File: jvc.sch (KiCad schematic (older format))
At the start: 14 parts, among them J1 AV PCB, J2 Main PCB, J3 VGA, SW1 SW_SPST

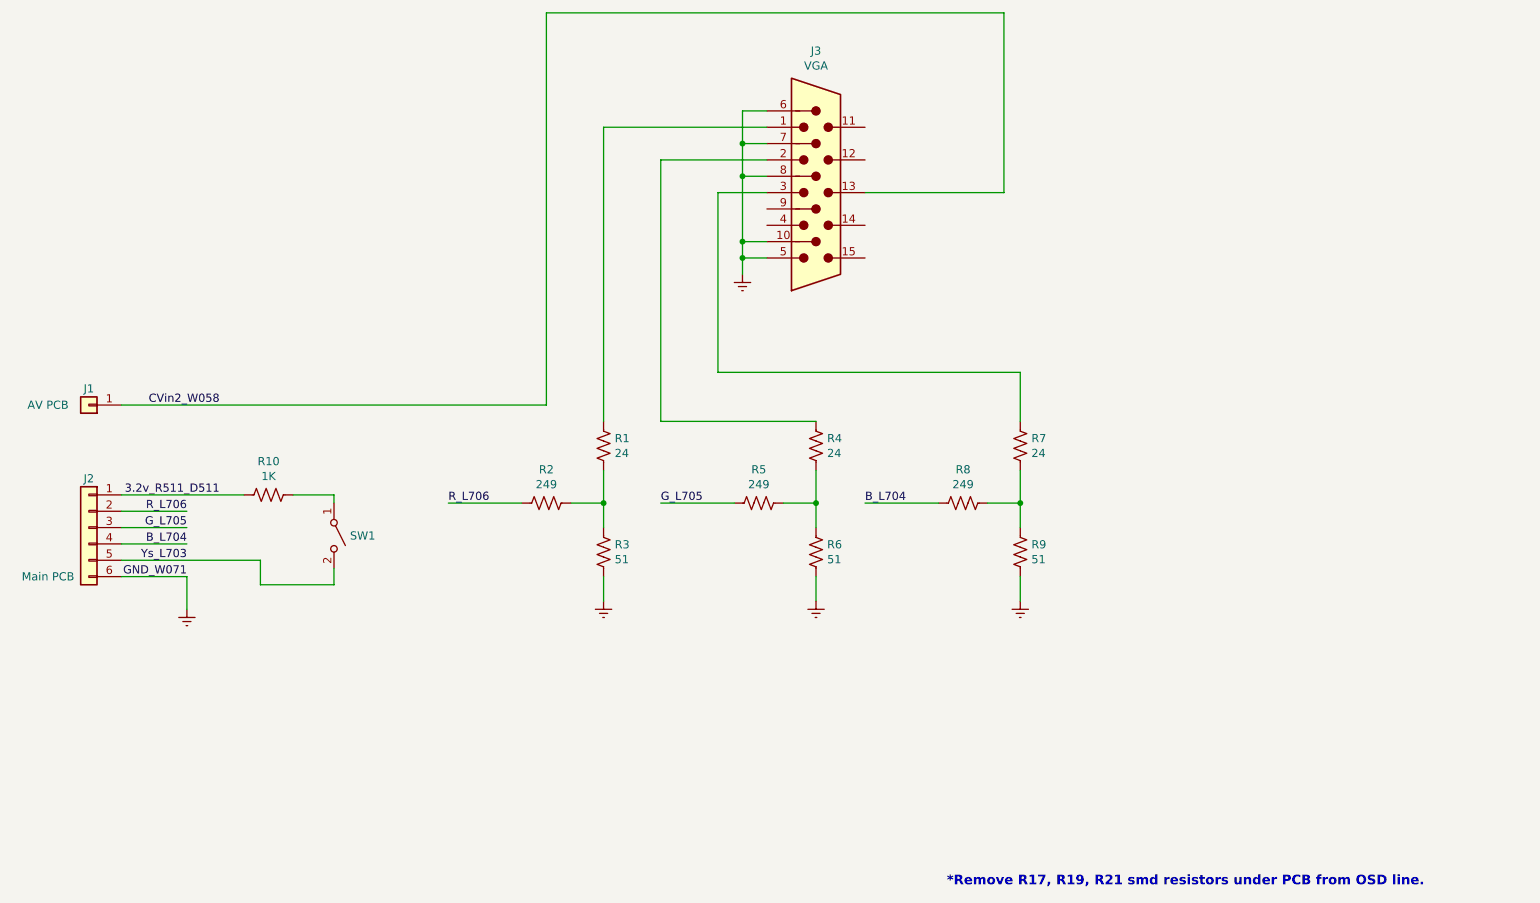
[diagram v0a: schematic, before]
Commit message: Turnout Not 0.5Vpp
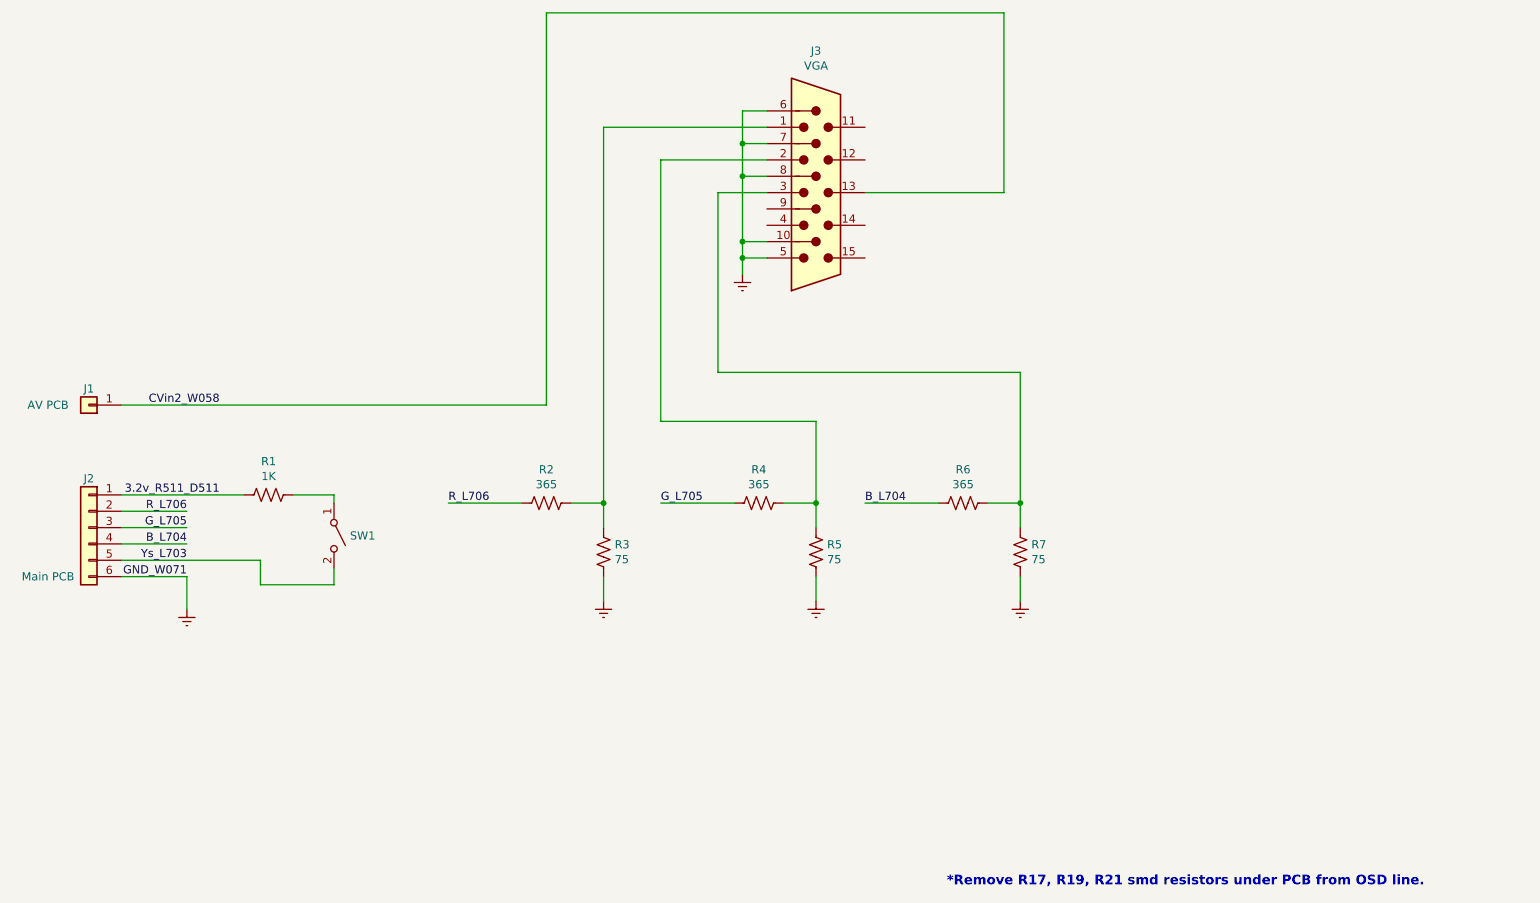
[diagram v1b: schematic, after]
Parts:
- removed R1, R4, R7: 24, symbol Device:R_US
- R2: value 249 -> 365
- R3: value 51 -> 75
- R4: renamed from R5; value 249 -> 365
- R5: renamed from R6; value 51 -> 75
- R6: renamed from R8; value 249 -> 365
- R7: renamed from R9; value 51 -> 75
- renumbered R10 to R1
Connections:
- net at J3.1: now also R2.1, R3.1
- net at J3.3: now also R6.1, R7.1
- net at J3.2: now also R4.1, R5.1
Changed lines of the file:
@@
 $EndDescr
-$Comp
-L Device:R_US R1
-U 1 1 5E6B4719
-P 4950 4000
-F 0 "R1" H 5018 4046 50  0000 L CNN
-F 1 "24" H 5018 3955 50  0000 L CNN
-F 2 "" V 4990 3990 50  0001 C CNN
-F 3 "~" H 4950 4000 50  0001 C CNN
-	1    4950 4000
-	1    0    0    -1
-$EndComp
 $Comp
 L Device:R_US R2
@@
 P 4600 4350
 F 0 "R2" V 4395 4350 50  0000 C CNN
-F 1 "249" V 4486 4350 50  0000 C CNN
+F 1 "365" V 4486 4350 50  0000 C CNN
 F 2 "" V 4640 4340 50  0001 C CNN
 F 3 "~" H 4600 4350 50  0001 C CNN
@@
 P 4950 4650
 F 0 "R3" H 5018 4696 50  0000 L CNN
-F 1 "51" H 5018 4605 50  0000 L CNN
+F 1 "75" H 5018 4605 50  0000 L CNN
 F 2 "" V 4990 4640 50  0001 C CNN
 F 3 "~" H 4950 4650 50  0001 C CNN
@@
 	1    0    0    -1
 $EndComp
-Wire Wire Line
-	4950 4150 4950 4350
 Connection ~ 4950 4350
 Wire Wire Line
@@
 $EndComp
 $Comp
-L Device:R_US R7
-U 1 1 5E6CEC38
-P 7500 4000
-F 0 "R7" H 7568 4046 50  0000 L CNN
-F 1 "24" H 7568 3955 50  0000 L CNN
-F 2 "" V 7540 3990 50  0001 C CNN
-F 3 "~" H 7500 4000 50  0001 C CNN
-	1    7500 4000
-	1    0    0    -1
-$EndComp
-$Comp
-L Device:R_US R8
+L Device:R_US R6
 U 1 1 5E6CEC42
 P 7150 4350
-F 0 "R8" V 6945 4350 50  0000 C CNN
-F 1 "249" V 7036 4350 50  0000 C CNN
+F 0 "R6" V 6945 4350 50  0000 C CNN
+F 1 "365" V 7036 4350 50  0000 C CNN
 F 2 "" V 7190 4340 50  0001 C CNN
 F 3 "~" H 7150 4350 50  0001 C CNN
@@
 $EndComp
 $Comp
-L Device:R_US R9
+L Device:R_US R7
 U 1 1 5E6CEC4C
 P 7500 4650
-F 0 "R9" H 7568 4696 50  0000 L CNN
-F 1 "51" H 7568 4605 50  0000 L CNN
+F 0 "R7" H 7568 4696 50  0000 L CNN
+F 1 "75" H 7568 4605 50  0000 L CNN
 F 2 "" V 7540 4640 50  0001 C CNN
 F 3 "~" H 7500 4650 50  0001 C CNN
@@
 	1    0    0    -1
 $EndComp
-Wire Wire Line
-	7500 4150 7500 4350
 Connection ~ 7500 4350
 Wire Wire Line
@@
 	7300 4350 7500 4350
 $Comp
-L Device:R_US R4
-U 1 1 5E6D13FF
-P 6250 4000
-F 0 "R4" H 6318 4046 50  0000 L CNN
-F 1 "24" H 6318 3955 50  0000 L CNN
-F 2 "" V 6290 3990 50  0001 C CNN
-F 3 "~" H 6250 4000 50  0001 C CNN
-	1    6250 4000
-	1    0    0    -1
-$EndComp
-$Comp
 L Device:R_US R5
-U 1 1 5E6D1409
-P 5900 4350
-F 0 "R5" V 5695 4350 50  0000 C CNN
-F 1 "249" V 5786 4350 50  0000 C CNN
-F 2 "" V 5940 4340 50  0001 C CNN
-F 3 "~" H 5900 4350 50  0001 C CNN
-	1    5900 4350
-	0    1    1    0
-$EndComp
-$Comp
-L Device:R_US R6
 U 1 1 5E6D1413
 P 6250 4650
-F 0 "R6" H 6318 4696 50  0000 L CNN
-F 1 "51" H 6318 4605 50  0000 L CNN
+F 0 "R5" H 6318 4696 50  0000 L CNN
+F 1 "75" H 6318 4605 50  0000 L CNN
 F 2 "" V 6290 4640 50  0001 C CNN
 F 3 "~" H 6250 4650 50  0001 C CNN
@@
 	1    0    0    -1
 $EndComp
-Wire Wire Line
-	6250 4150 6250 4350
 Connection ~ 6250 4350
 Wire Wire Line
@@
 $EndComp
 Wire Wire Line
-	4950 3850 4950 2050
-Wire Wire Line
 	4950 2050 5950 2050
 Wire Wire Line
@@
 Wire Wire Line
 	5300 2250 5950 2250
-Wire Wire Line
-	7500 3850 7500 3550
 Wire Wire Line
 	7500 3550 5650 3550
@@
 $EndComp
 $Comp
-L Device:R_US R10
+L Device:R_US R1
 U 1 1 5E712B9B
 P 2900 4300
-F 0 "R10" V 2695 4300 50  0000 C CNN
+F 0 "R1" V 2695 4300 50  0000 C CNN
 F 1 "1K" V 2786 4300 50  0000 C CNN
 F 2 "" V 2940 4290 50  0001 C CNN
@@
 	5800 1950 5800 2150
 Connection ~ 5800 2150
+Wire Wire Line
+	7500 3550 7500 4350
+Wire Wire Line
+	6250 3850 6250 4350
+Wire Wire Line
+	4950 2050 4950 4350
+$Comp
+L Device:R_US R4
+U 1 1 5E6D1409
+P 5900 4350
+F 0 "R4" V 5695 4350 50  0000 C CNN
+F 1 "365" V 5786 4350 50  0000 C CNN
+F 2 "" V 5940 4340 50  0001 C CNN
+F 3 "~" H 5900 4350 50  0001 C CNN
+	1    5900 4350
+	0    1    1    0
+$EndComp
 $EndSCHEMATC

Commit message: Move RGB on input 1 and DPDT sw enable CVBS input in RGB mode for csync
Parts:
- removed SW1: SW_SPST, symbol Switch:SW_SPST
- added SW1: SW_DPST, symbol Switch:SW_DPST
- J1: symbol Connector_Generic:Conn_01x01 -> Connector_Generic:Conn_01x04
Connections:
- net GNDREF: now also J1.1 (Pin_1)
- net Ys_L703: now also SW1.2
- net at R1.1: now also SW1.1
- net CVin2_W058 renamed CVin1_D815
- net CVin1_D815: now also J1.4 (Pin_4); no longer J1.1 (Pin_1)
- new net S-Video_J801pin5: J1.3 (Pin_3), SW1.4
- new net S-Video_J801pin6: J1.2 (Pin_2), SW1.3
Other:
- note added: "SW1 toggle between\nS-Video & RGB\nBoth share same audio in"
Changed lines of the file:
@@
 B_L704
 $Comp
-L Connector_Generic:Conn_01x01 J1
+L Connector_Generic:Conn_01x04 J1
 U 1 1 5E6BABC1
 P 1800 3750
-F 0 "J1" H 1800 3650 50  0000 C CNN
+F 0 "J1" H 1800 3450 50  0000 C CNN
 F 1 "AV PCB" H 2050 3750 50  0000 C CNN
 F 2 "" H 1800 3750 50  0001 C CNN
@@
 Wire Wire Line
 	2000 4800 2400 4800
-Text Label 2600 3750 2    50   ~ 0
-CVin2_W058
+Text Label 2600 3550 2    50   ~ 0
+CVin1_D815
 Wire Wire Line
 	4750 4350 4950 4350
@@
 	5650 2450 5950 2450
 Wire Wire Line
-	4600 3750 4600 1350
-Wire Wire Line
 	4600 1350 7400 1350
 Wire Wire Line
@@
 	7400 2450 6550 2450
 Wire Wire Line
-	2000 3750 4600 3750
+	2000 3550 4600 3550
 Text Notes 7050 6700 0    59   ~ 12
 *Remove R17, R19, R21 smd resistors under PCB from OSD line.
-$Comp
-L Switch:SW_SPST SW1
-U 1 1 5E711972
-P 3300 4550
-F 0 "SW1" V 3300 4648 50  0000 L CNN
-F 1 "SW_SPST" V 3345 4648 50  0001 L CNN
-F 2 "" H 3300 4550 50  0001 C CNN
-F 3 "~" H 3300 4550 50  0001 C CNN
-	1    3300 4550
-	0    1    1    0
-$EndComp
 $Comp
 L Device:R_US R1
@@
 	2000 4300 2750 4300
 Wire Wire Line
-	3050 4300 3300 4300
-Wire Wire Line
-	3300 4300 3300 4350
-Wire Wire Line
-	2850 4700 2850 4850
-Wire Wire Line
-	2850 4850 3300 4850
-Wire Wire Line
-	3300 4850 3300 4750
-Wire Wire Line
-	2000 4700 2850 4700
-Wire Wire Line
 	5950 2350 5800 2350
 $Comp
@@
 	0    1    1    0
 $EndComp
+$Comp
+L Switch:SW_DPST SW1
+U 1 1 5E8D0B90
+P 3400 4200
+F 0 "SW1" H 3400 4525 50  0000 C CNN
+F 1 "SW_DPST" H 3400 4434 50  0000 C CNN
+F 2 "" H 3400 4200 50  0001 C CNN
+F 3 "~" H 3400 4200 50  0001 C CNN
+	1    3400 4200
+	1    0    0    -1
+$EndComp
+$Comp
+L power:GNDREF #PWR?
+U 1 1 5E8D572D
+P 2400 4000
+F 0 "#PWR?" H 2400 3750 50  0001 C CNN
+F 1 "GNDREF" H 2405 3827 50  0001 C CNN
+F 2 "" H 2400 4000 50  0001 C CNN
+F 3 "" H 2400 4000 50  0001 C CNN
+	1    2400 4000
+	1    0    0    -1
+$EndComp
+Wire Wire Line
+	2400 3850 2400 4000
+Wire Wire Line
+	2000 3850 2400 3850
+Wire Wire Line
+	3050 4300 3200 4300
+Wire Wire Line
+	3600 4700 3600 4300
+Wire Wire Line
+	2000 4700 3600 4700
+Wire Wire Line
+	4600 3550 4600 1350
+Wire Wire Line
+	2000 3650 3600 3650
+Wire Wire Line
+	3600 3650 3600 4100
+Wire Wire Line
+	2000 3750 3200 3750
+Wire Wire Line
+	3200 3750 3200 4100
+Text Label 2150 3650 0    50   ~ 0
+S-Video_J801pin5
+Text Label 2150 3750 0    50   ~ 0
+S-Video_J801pin6
+Text Label 2150 3850 0    50   ~ 0
+GND_D816
+Text Notes 3650 4000 0    50   ~ 10
+SW1 toggle between\nS-Video & RGB\nBoth share same audio in
 $EndSCHEMATC
